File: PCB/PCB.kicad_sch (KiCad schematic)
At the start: 91 parts, among them J1 USB_B_Micro, J2 Conn_01x02, Q1 PJA3428, Q2 PJA3428, Q3 AO3401A, SW1 SW_Push, SW2 SW_Push, SW3 SW_Push, SW4 ON/OFF, U1 ESP32-PICO-MINI-02, U2 CP2102N-Axx-xQFN24, U3 TP4056, U4 TPS63070RNMR, U5 BNO080, Y1 32.768 kHz, Y2 32.768 kHz

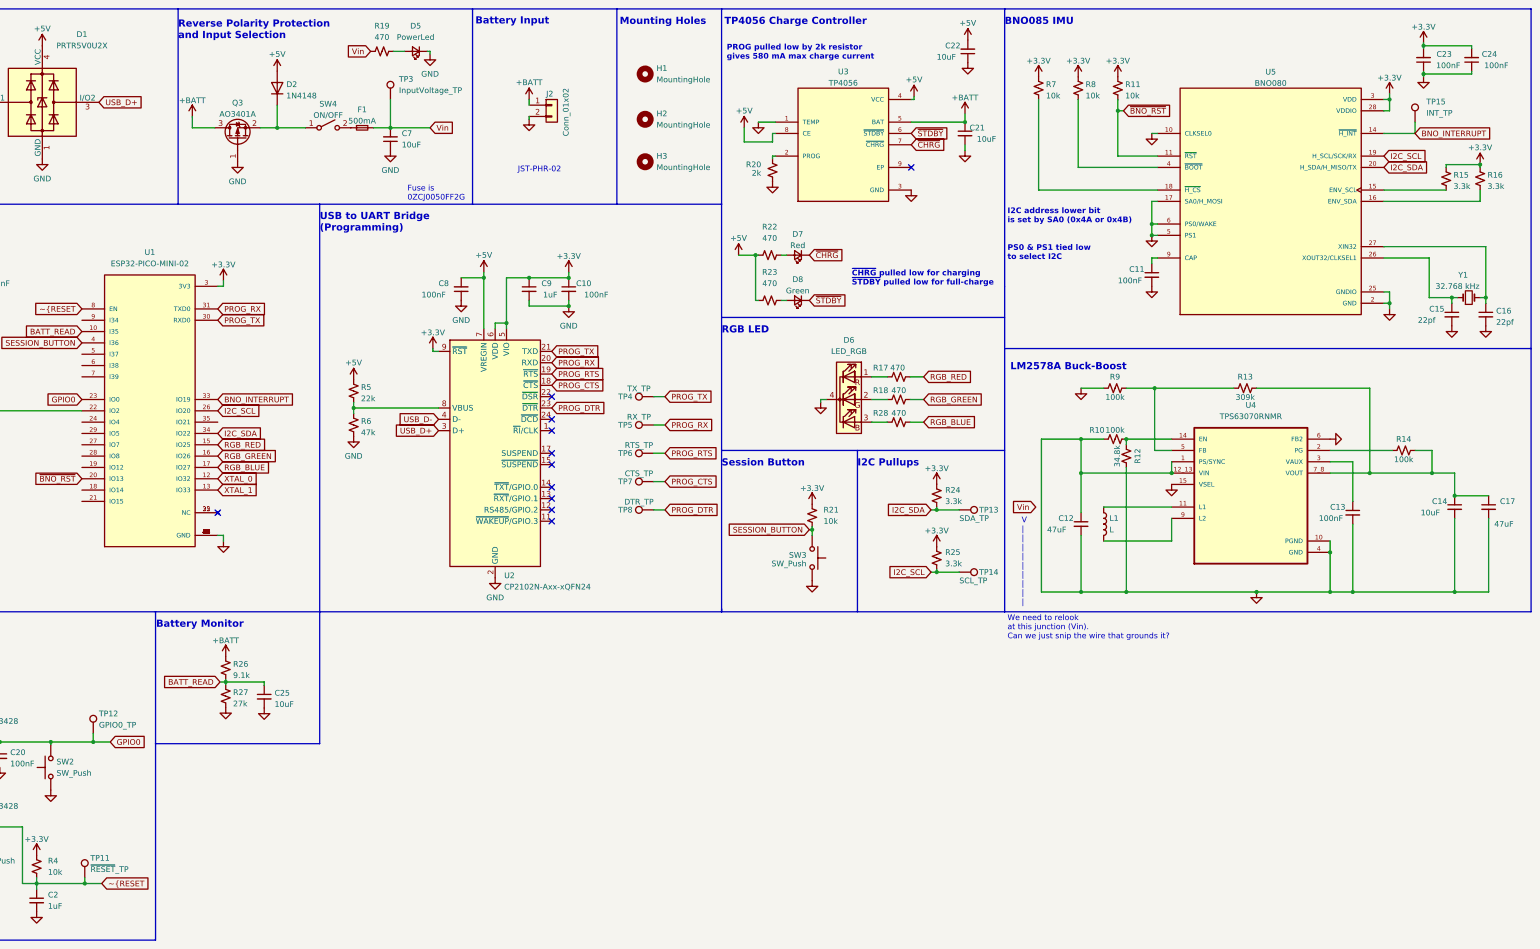
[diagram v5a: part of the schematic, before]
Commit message: huuuge rerouting and replacement. Added ESD protection resistors
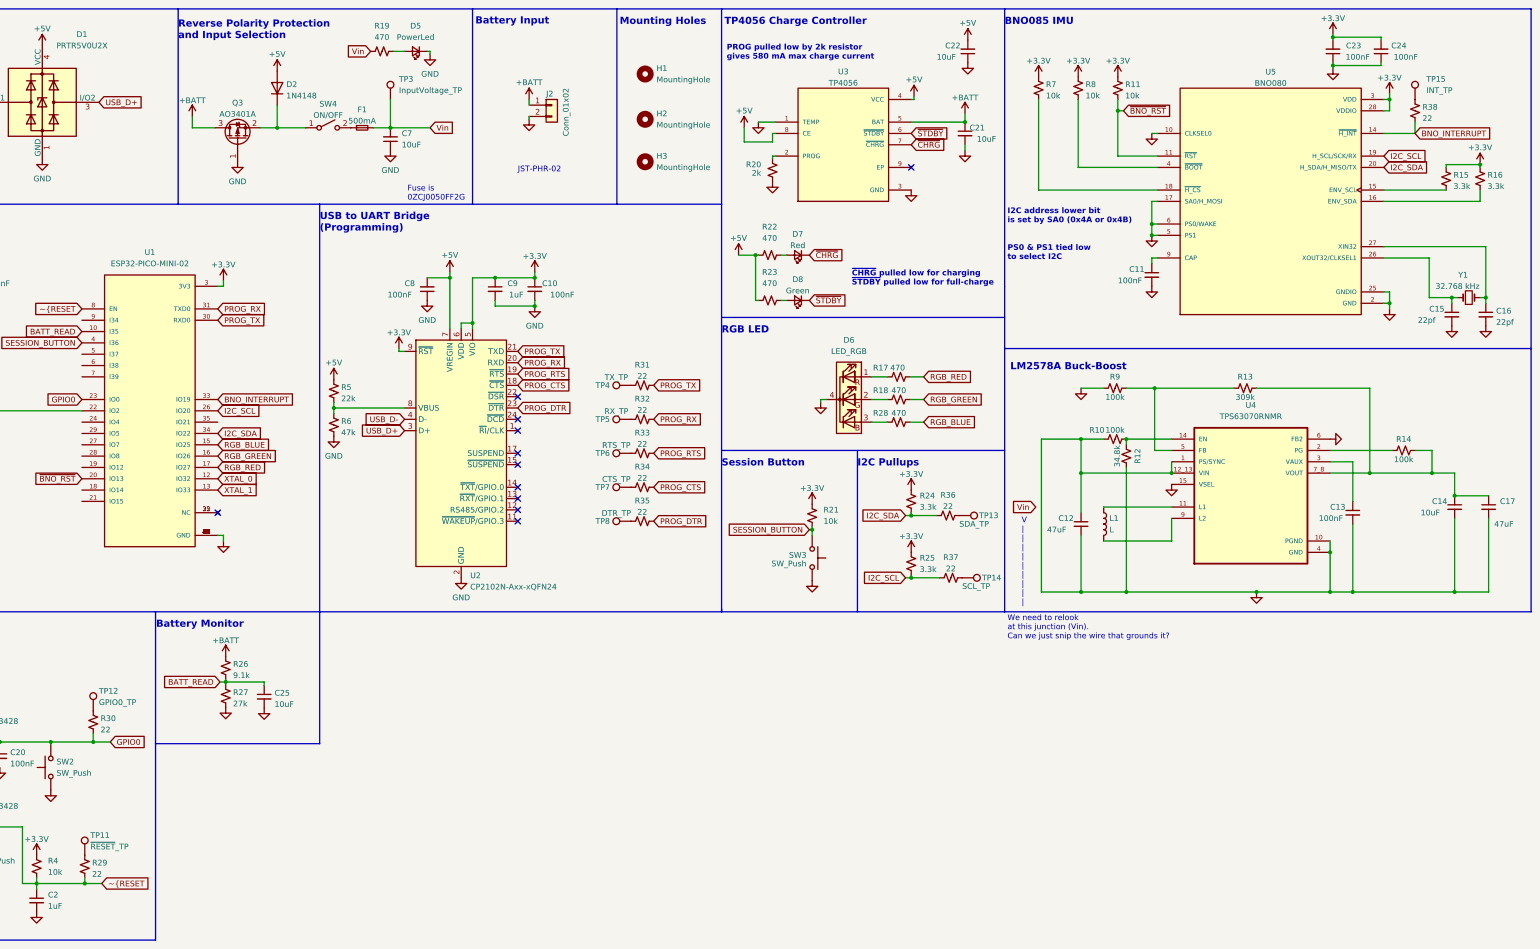
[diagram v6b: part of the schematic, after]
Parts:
- added R29, R30, R31, R32, R33, R34, R35, R36, R37, R38: 22, Resistor_SMD:R_0603_1608Metric, symbol Device:R_Small_US
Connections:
- net BNO_INTERRUPT: now also R38.1; no longer TP15.1
- net GPIO0: now also R30.2; no longer TP12.1
- net I2C_SCL: now also R37.1; no longer TP14.1
- net I2C_SDA: now also R36.1; no longer TP13.1
- net PROG_CTS: now also R34.2; no longer TP7.1
- net PROG_DTR: now also R35.2; no longer TP8.1
- net PROG_RTS: now also R33.2; no longer TP6.1
- net PROG_RX: now also R32.2; no longer TP5.1
- net PROG_TX: now also R31.2; no longer TP4.1
- net RGB_BLUE: now also U1.15 (IO25); no longer U1.17 (IO27)
- net RGB_RED: now also U1.17 (IO27); no longer U1.15 (IO25)
- net ~{RESET: now also R29.2; no longer TP11.1
- new net: R35.1, TP8.1
- new net: R37.2, TP14.1
- new net: R34.1, TP7.1
- new net: R38.2, TP15.1
- new net: R30.1, TP12.1
- new net: R33.1, TP6.1
- new net: R36.2, TP13.1
- new net: R31.1, TP4.1
- new net: R29.1, TP11.1
- new net: R32.1, TP5.1
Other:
- moved on the sheet: C10, C23, C24, C8, C9, R24, R25, R5, R6, TP11, TP12, TP13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

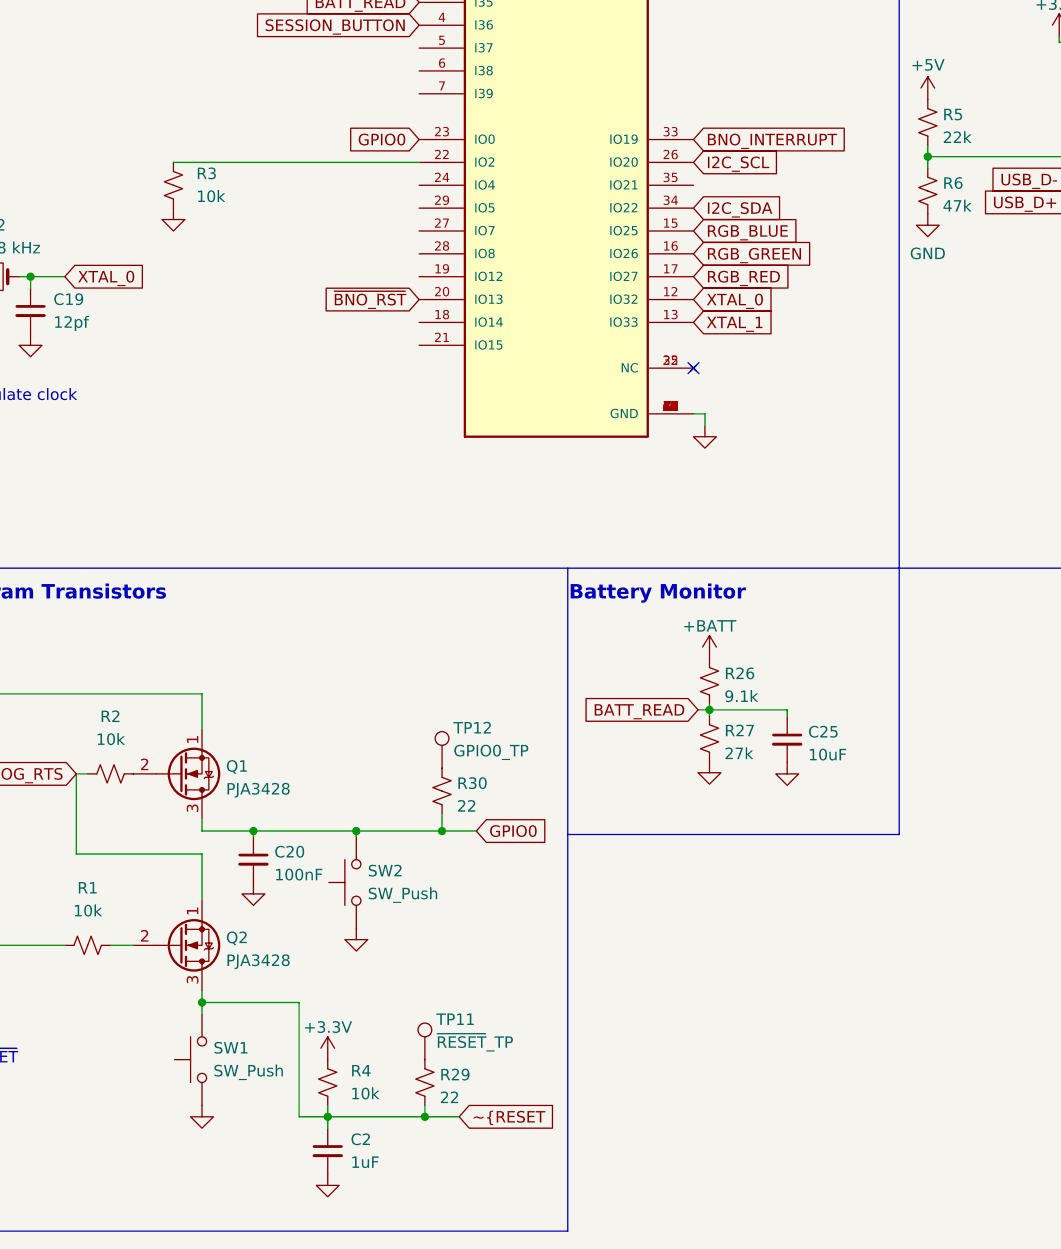
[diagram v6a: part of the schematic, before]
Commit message: add JTAG support
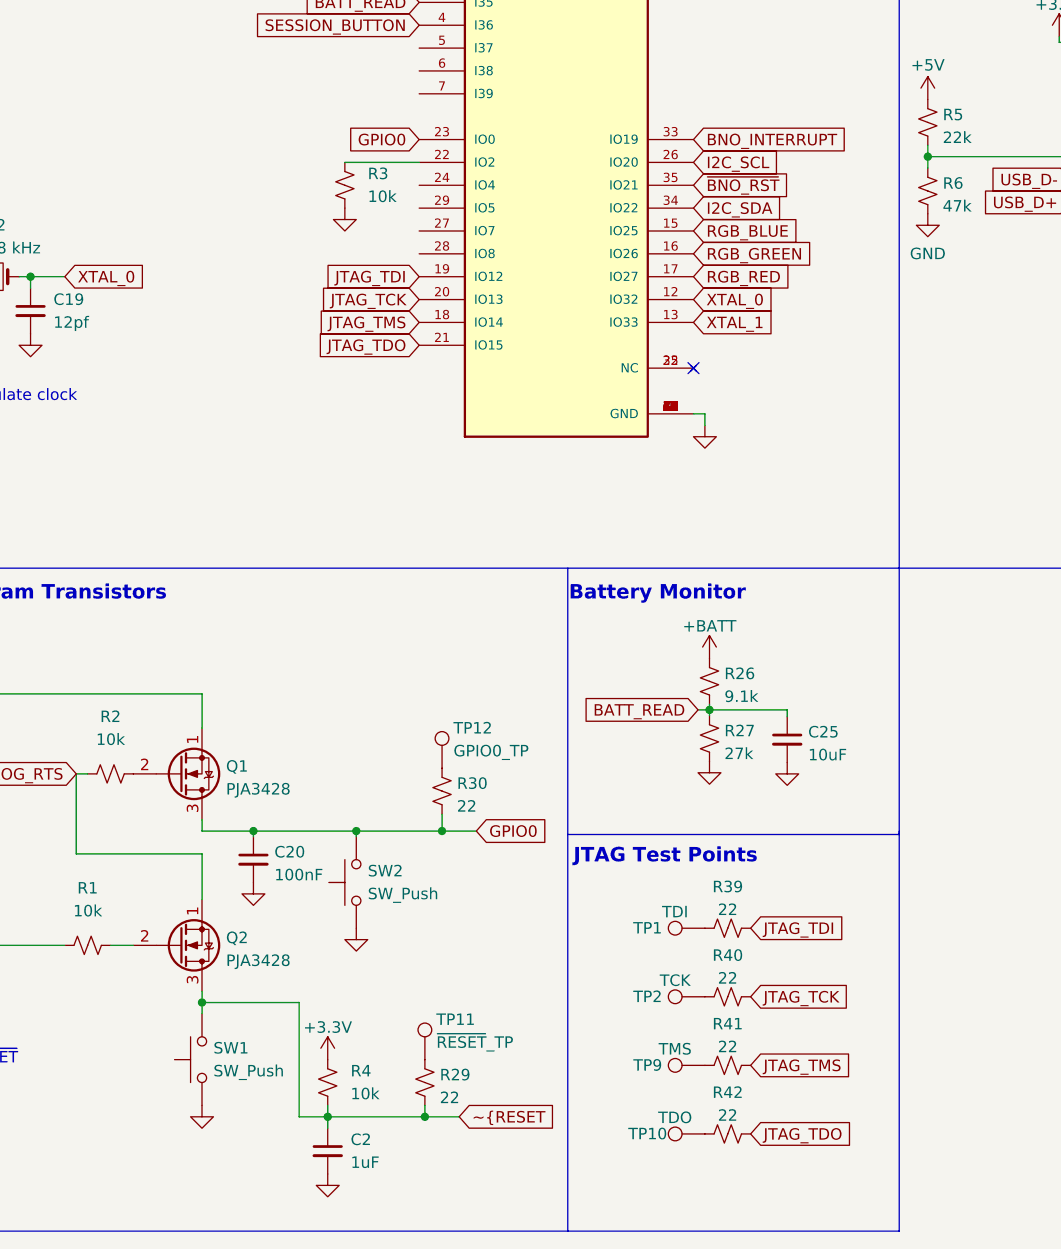
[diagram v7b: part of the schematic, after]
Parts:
- added R39, R40, R41, R42: 22, Resistor_SMD:R_0603_1608Metric, symbol Device:R_Small_US
- added TP1: TDI, TestPoint:TestPoint_Pad_D1.0mm, symbol Connector:TestPoint
- added TP10: TDO, TestPoint:TestPoint_Pad_D1.0mm, symbol Connector:TestPoint
- added TP2: TCK, TestPoint:TestPoint_Pad_D1.0mm, symbol Connector:TestPoint
- added TP9: TMS, TestPoint:TestPoint_Pad_D1.0mm, symbol Connector:TestPoint
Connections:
- net ~{BNO_RST}: now also U1.35 (IO21); no longer U1.20 (IO13)
- net JTAG_TMS: now reaches U1.18 (IO14)
- net JTAG_TMS: now also R41.2
- net JTAG_TDI: now reaches U1.19 (IO12)
- net JTAG_TDI: now also R39.2
- net JTAG_TDO: now reaches U1.21 (IO15)
- net JTAG_TDO: now also R42.2
- new net: R39.1, TP1.1
- new net: R40.1, TP2.1
- new net: R42.1, TP10.1
- new net: R41.1, TP9.1
- new net JTAG_TCK: R40.2, U1.20 (IO13)
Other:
- note added: "JTAG Test Points"
- moved on the sheet: R3
